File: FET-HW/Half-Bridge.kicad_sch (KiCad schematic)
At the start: 6 parts

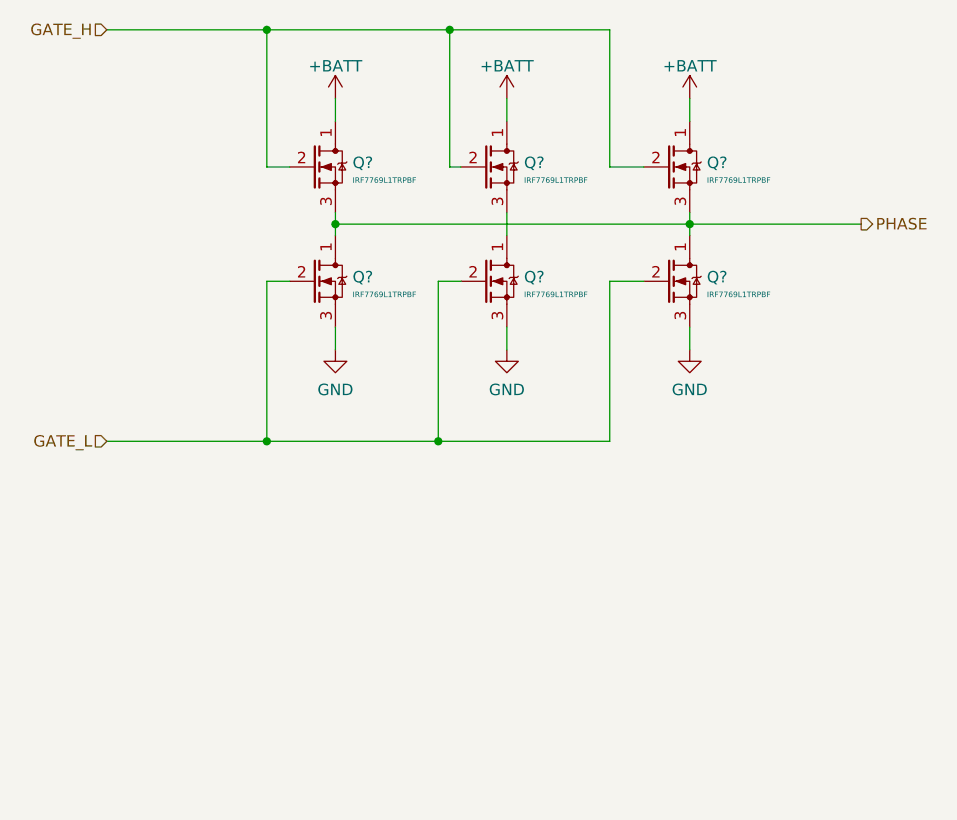
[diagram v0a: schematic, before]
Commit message: First pass at FET PCB layout
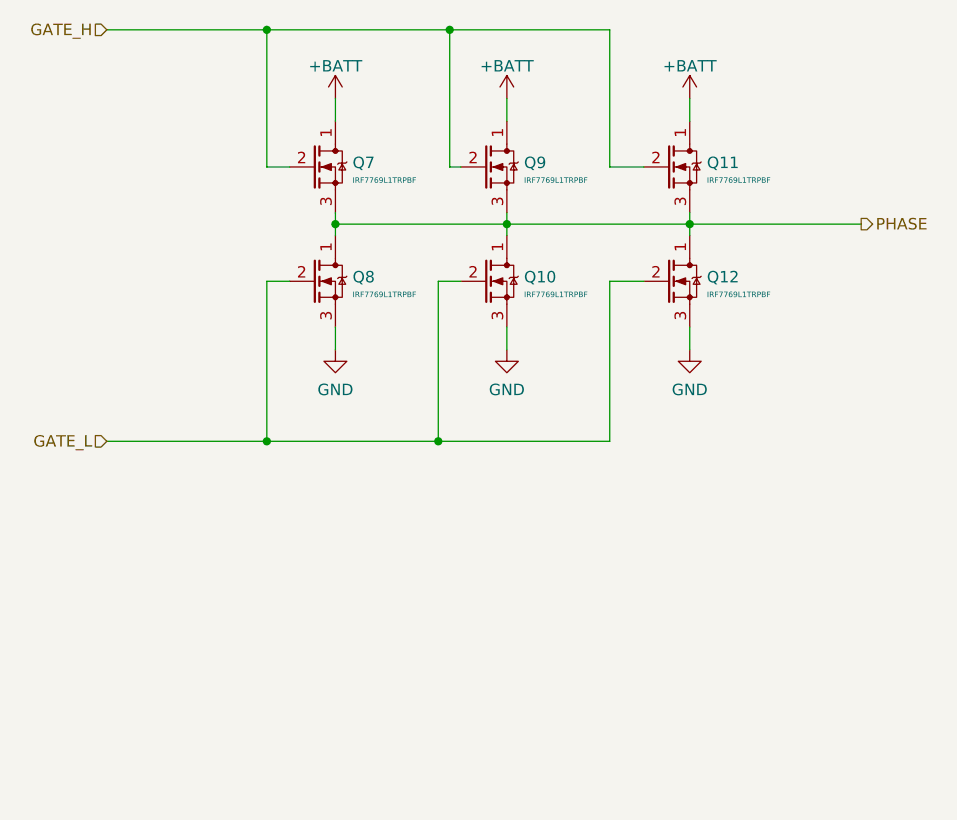
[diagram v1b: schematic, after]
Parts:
- gave numbers to parts that had none: 6
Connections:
- net PHASE: now also Q10.1 (D), Q9.3 (S)
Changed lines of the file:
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@@
   (junction (at 106.68 43.18) (diameter 0) (color 0 0 0 0)
   )
+  (junction (at 114.3 64.77) (diameter 0) (color 0 0 0 0)
+  )
   (junction (at 106.68 88.9) (diameter 0) (color 0 0 0 0)
   )
+  (junction (at 133.35 64.77) (diameter 0) (color 0 0 0 0)
+  )
   (junction (at 125.73 88.9) (diameter 0) (color 0 0 0 0)
   )
-  (junction (at 114.3 64.77) (diameter 0) (color 0 0 0 0)
-  )
   (junction (at 127 43.18) (diameter 0) (color 0 0 0 0)
   )
@@
     (stroke (width 0) (type default) (color 0 0 0 0))
   )
+  (wire (pts (xy 133.35 64.77) (xy 153.67 64.77))
+    (stroke (width 0) (type default) (color 0 0 0 0))
+  )
+  (wire (pts (xy 114.3 63.5) (xy 114.3 64.77))
+    (stroke (width 0) (type default) (color 0 0 0 0))
+  )
+  (wire (pts (xy 153.67 63.5) (xy 153.67 64.77))
+    (stroke (width 0) (type default) (color 0 0 0 0))
+  )
+  (wire (pts (xy 106.68 71.12) (xy 106.68 88.9))
+    (stroke (width 0) (type default) (color 0 0 0 0))
+  )
+  (wire (pts (xy 144.78 71.12) (xy 144.78 88.9))
+    (stroke (width 0) (type default) (color 0 0 0 0))
+  )
+  (wire (pts (xy 133.35 64.77) (xy 133.35 66.04))
+    (stroke (width 0) (type default) (color 0 0 0 0))
+  )
+  (wire (pts (xy 114.3 64.77) (xy 133.35 64.77))
+    (stroke (width 0) (type default) (color 0 0 0 0))
+  )
+  (wire (pts (xy 127 43.18) (xy 144.78 43.18))
+    (stroke (width 0) (type default) (color 0 0 0 0))
+  )
+  (wire (pts (xy 106.68 88.9) (xy 125.73 88.9))
+    (stroke (width 0) (type default) (color 0 0 0 0))
+  )
+  (wire (pts (xy 109.22 71.12) (xy 106.68 71.12))
+    (stroke (width 0) (type default) (color 0 0 0 0))
+  )
+  (wire (pts (xy 106.68 43.18) (xy 127 43.18))
+    (stroke (width 0) (type default) (color 0 0 0 0))
+  )
   (wire (pts (xy 114.3 64.77) (xy 114.3 66.04))
     (stroke (width 0) (type default) (color 0 0 0 0))
   )
-  (wire (pts (xy 153.67 63.5) (xy 153.67 64.77))
-    (stroke (width 0) (type default) (color 0 0 0 0))
-  )
-  (wire (pts (xy 106.68 71.12) (xy 106.68 88.9))
-    (stroke (width 0) (type default) (color 0 0 0 0))
-  )
-  (wire (pts (xy 144.78 71.12) (xy 144.78 88.9))
-    (stroke (width 0) (type default) (color 0 0 0 0))
-  )
-  (wire (pts (xy 127 43.18) (xy 144.78 43.18))
-    (stroke (width 0) (type default) (color 0 0 0 0))
-  )
-  (wire (pts (xy 114.3 64.77) (xy 153.67 64.77))
-    (stroke (width 0) (type default) (color 0 0 0 0))
-  )
-  (wire (pts (xy 106.68 88.9) (xy 125.73 88.9))
-    (stroke (width 0) (type default) (color 0 0 0 0))
-  )
-  (wire (pts (xy 109.22 71.12) (xy 106.68 71.12))
-    (stroke (width 0) (type default) (color 0 0 0 0))
-  )
-  (wire (pts (xy 106.68 43.18) (xy 127 43.18))
-    (stroke (width 0) (type default) (color 0 0 0 0))
-  )
   (wire (pts (xy 148.59 58.42) (xy 144.78 58.42))
     (stroke (width 0) (type default) (color 0 0 0 0))
@@
     (stroke (width 0) (type default) (color 0 0 0 0))
   )
-  (wire (pts (xy 114.3 63.5) (xy 114.3 64.77))
-    (stroke (width 0) (type default) (color 0 0 0 0))
-  )
   (wire (pts (xy 127 43.18) (xy 127 58.42))
     (stroke (width 0) (type default) (color 0 0 0 0))
@@
     (stroke (width 0) (type default) (color 0 0 0 0))
   )
-  (wire (pts (xy 133.35 63.5) (xy 133.35 66.04))
+  (wire (pts (xy 133.35 63.5) (xy 133.35 64.77))
     (stroke (width 0) (type default) (color 0 0 0 0))
   )
@@
   (symbol (lib_id "Q_MOSFET:IRF7769L1TRPBF") (at 153.67 58.42 0) (unit 1)
     (in_bom yes) (on_board yes) (fields_autoplaced)
-    (property "Reference" "Q?" (id 0) (at 155.575 57.9533 0)
+    (property "Reference" "Q11" (id 0) (at 155.575 57.9533 0)
       (effects (font (size 1.27 1.27)) (justify left))
     )
@@
   (symbol (lib_id "Q_MOSFET:IRF7769L1TRPBF") (at 133.35 71.12 0) (unit 1)
     (in_bom yes) (on_board yes) (fields_autoplaced)
-    (property "Reference" "Q?" (id 0) (at 135.255 70.6533 0)
+    (property "Reference" "Q10" (id 0) (at 135.255 70.6533 0)
       (effects (font (size 1.27 1.27)) (justify left))
     )
@@
   (symbol (lib_id "Q_MOSFET:IRF7769L1TRPBF") (at 114.3 58.42 0) (unit 1)
     (in_bom yes) (on_board yes) (fields_autoplaced)
-    (property "Reference" "Q?" (id 0) (at 116.205 57.9533 0)
+    (property "Reference" "Q7" (id 0) (at 116.205 57.9533 0)
       (effects (font (size 1.27 1.27)) (justify left))
     )
@@
   (symbol (lib_id "power:GND") (at 153.67 78.74 0) (unit 1)
     (in_bom yes) (on_board yes) (fields_autoplaced)
-    (property "Reference" "#PWR?" (id 0) (at 153.67 85.09 0)
+    (property "Reference" "#PWR017" (id 0) (at 153.67 85.09 0)
       (effects (font (size 1.27 1.27)) hide)
     )
@@
   (symbol (lib_id "power:+BATT") (at 153.67 50.8 0) (unit 1)
     (in_bom yes) (on_board yes) (fields_autoplaced)
-    (property "Reference" "#PWR?" (id 0) (at 153.67 54.61 0)
+    (property "Reference" "#PWR016" (id 0) (at 153.67 54.61 0)
       (effects (font (size 1.27 1.27)) hide)
     )
@@
   (symbol (lib_id "Q_MOSFET:IRF7769L1TRPBF") (at 133.35 58.42 0) (unit 1)
     (in_bom yes) (on_board yes) (fields_autoplaced)
-    (property "Reference" "Q?" (id 0) (at 135.255 57.9533 0)
+    (property "Reference" "Q9" (id 0) (at 135.255 57.9533 0)
       (effects (font (size 1.27 1.27)) (justify left))
     )
@@
   (symbol (lib_id "power:GND") (at 133.35 78.74 0) (unit 1)
     (in_bom yes) (on_board yes) (fields_autoplaced)
-    (property "Reference" "#PWR?" (id 0) (at 133.35 85.09 0)
+    (property "Reference" "#PWR015" (id 0) (at 133.35 85.09 0)
       (effects (font (size 1.27 1.27)) hide)
     )
@@
   (symbol (lib_id "power:+BATT") (at 133.35 50.8 0) (unit 1)
     (in_bom yes) (on_board yes) (fields_autoplaced)
-    (property "Reference" "#PWR?" (id 0) (at 133.35 54.61 0)
+    (property "Reference" "#PWR014" (id 0) (at 133.35 54.61 0)
       (effects (font (size 1.27 1.27)) hide)
     )
@@
   (symbol (lib_id "power:GND") (at 114.3 78.74 0) (unit 1)
     (in_bom yes) (on_board yes) (fields_autoplaced)
-    (property "Reference" "#PWR?" (id 0) (at 114.3 85.09 0)
+    (property "Reference" "#PWR013" (id 0) (at 114.3 85.09 0)
       (effects (font (size 1.27 1.27)) hide)
     )
@@
   (symbol (lib_id "Q_MOSFET:IRF7769L1TRPBF") (at 114.3 71.12 0) (unit 1)
     (in_bom yes) (on_board yes) (fields_autoplaced)
-    (property "Reference" "Q?" (id 0) (at 116.205 70.6533 0)
+    (property "Reference" "Q8" (id 0) (at 116.205 70.6533 0)
       (effects (font (size 1.27 1.27)) (justify left))
     )
@@
   (symbol (lib_id "Q_MOSFET:IRF7769L1TRPBF") (at 153.67 71.12 0) (unit 1)
     (in_bom yes) (on_board yes) (fields_autoplaced)
-    (property "Reference" "Q?" (id 0) (at 155.575 70.6533 0)
+    (property "Reference" "Q12" (id 0) (at 155.575 70.6533 0)
       (effects (font (size 1.27 1.27)) (justify left))
     )
@@
   (symbol (lib_id "power:+BATT") (at 114.3 50.8 0) (unit 1)
     (in_bom yes) (on_board yes) (fields_autoplaced)
-    (property "Reference" "#PWR?" (id 0) (at 114.3 54.61 0)
-      (effects (font (size 1.27 1.27)) hide)
-    )
+    (property "Reference" "#PWR012" (id 0) (at 114.3 54.61 0)
+      (effects (font (size 1.27 1.27)) hide)
+    )

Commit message: Add in some capacitance
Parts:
- added C10, C11, C12, C7, C8, C9: 4u7,100v, C_Capacitor:C_1206, symbol C_Capacitor:C_1206
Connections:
- net +BATT: now also C10.1, C11.1, C12.1, C7.1, C8.1, C9.1
- net GND: now also C10.2, C11.2, C12.2, C7.2, C8.2, C9.2
